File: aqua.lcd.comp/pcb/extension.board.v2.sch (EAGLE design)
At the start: 50 parts, among them IC1 NCP1117ST50T3G, K2 JS-M1-9V-4, Q1 BC447, T1 IRFR024NPBF, T10 BC847BSMD, T11 IRFR024NPBF, T12 BC847BSMD, T2 BC847BSMD, T3 IRFR024NPBF, T4 BC847BSMD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

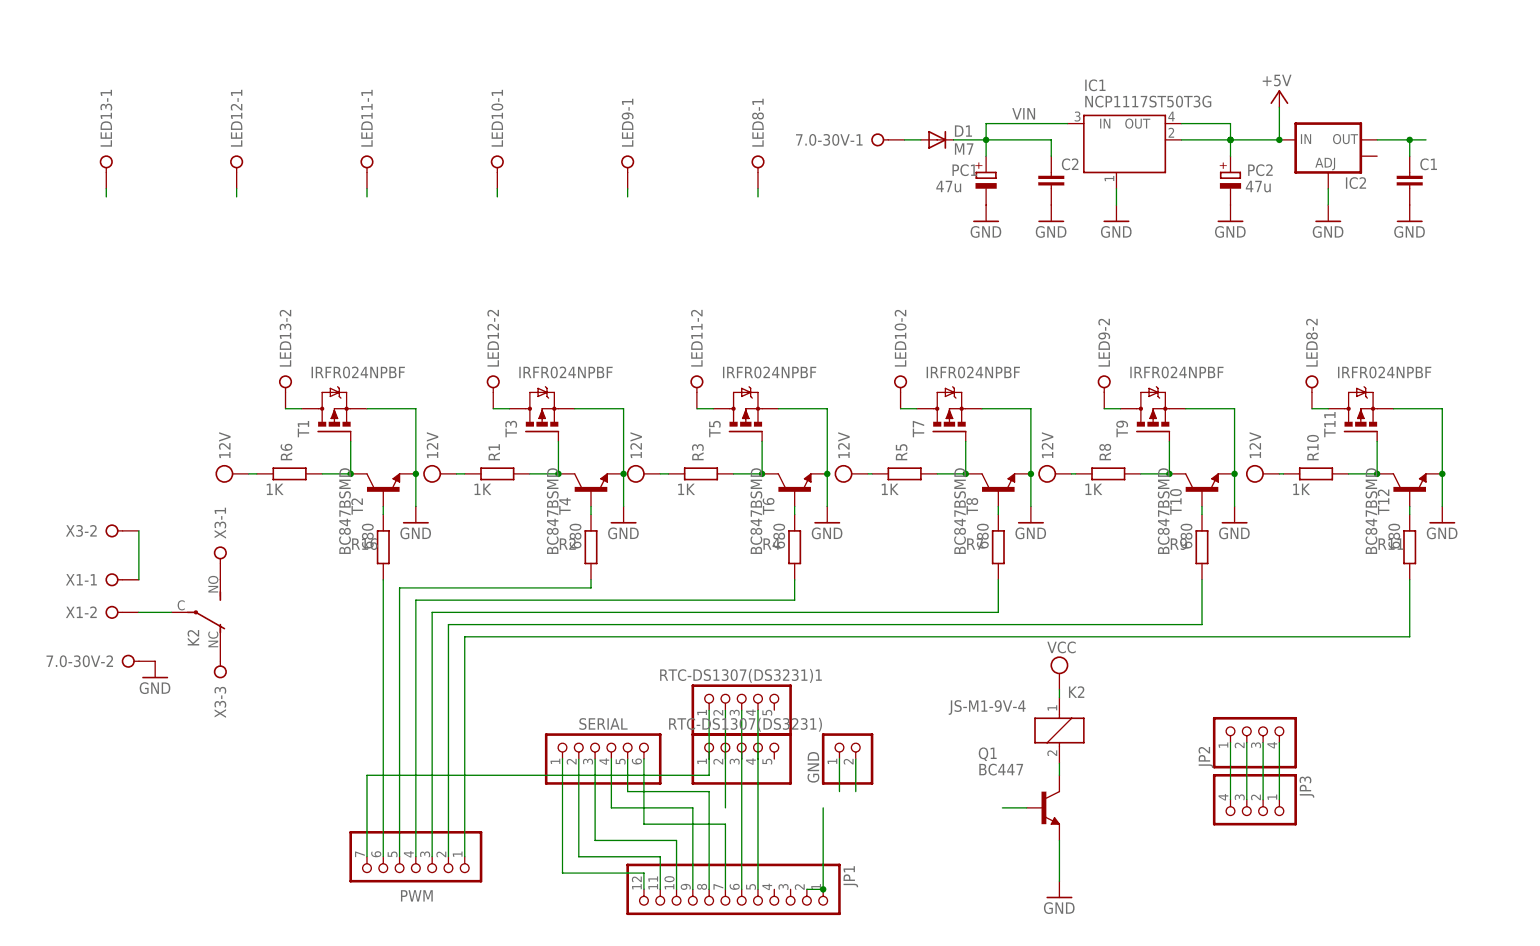
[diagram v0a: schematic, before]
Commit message: extension board modified
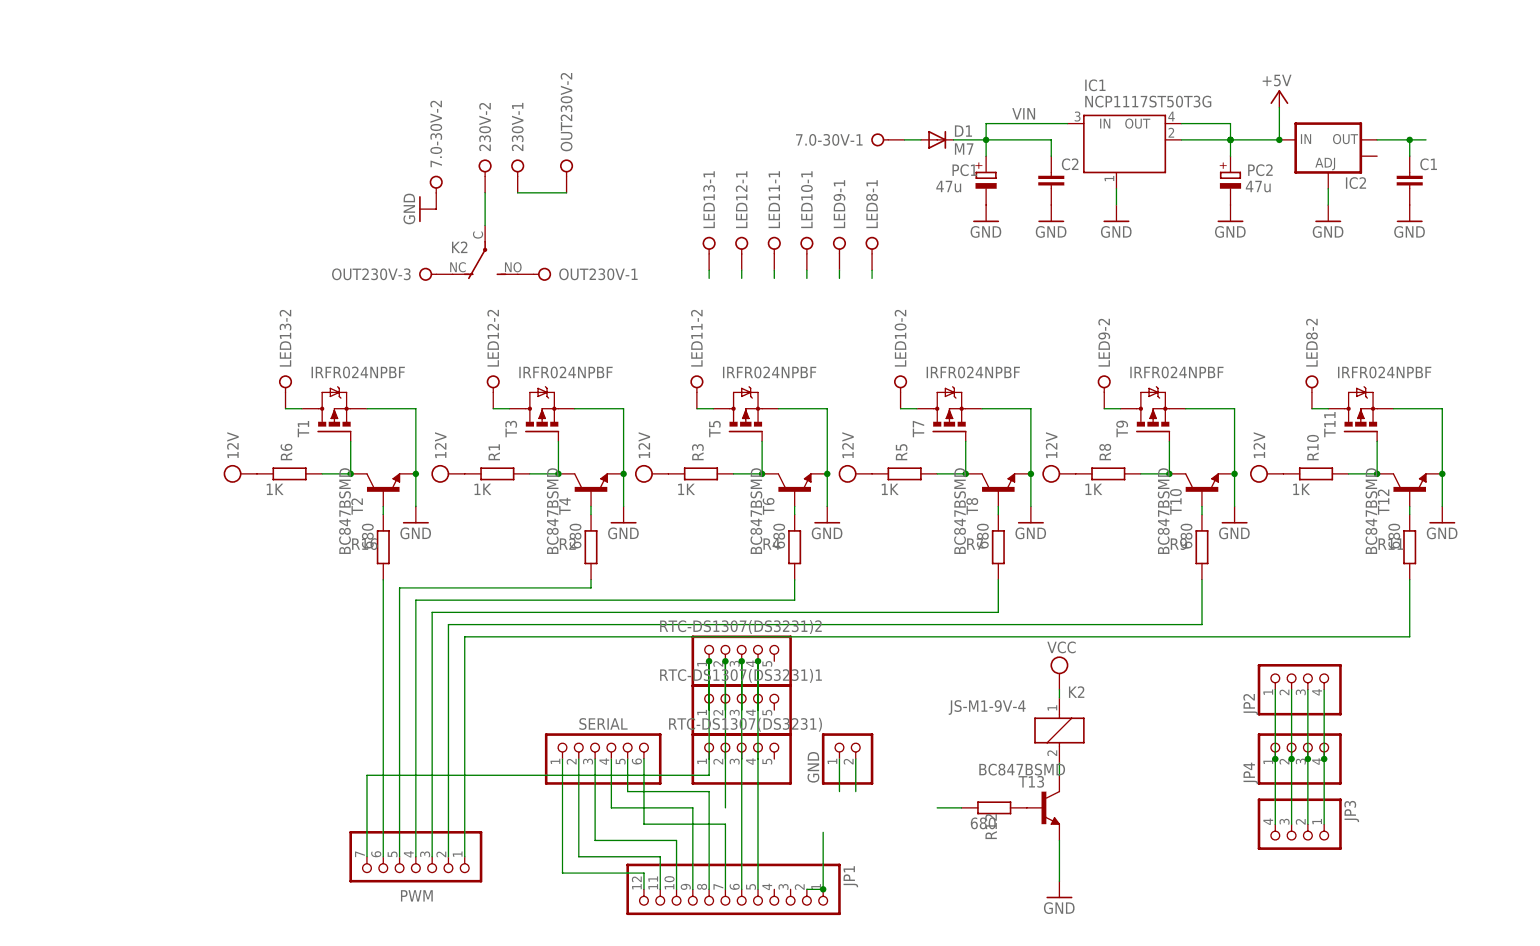
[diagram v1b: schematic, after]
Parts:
- removed Q1: BC447, transistor-npn:BC447
- removed X1: (no value), con-wago-508:W237-02P
- removed X3: (no value), con-wago-508:W237-3E
- added 230V: (no value), con-wago-508:W237-02P
- added JP4: (no value), pinhead:PINHD-1X4
- added OUT230V: (no value), con-wago-508:W237-3E
- added R12: 680, rcl:R-EU_R1206
- added RTC-DS1307(DS3231)2: (no value), pinhead:PINHD-1X5
- added T13: BC847BSMD, transistor-npn:BC847BSMD
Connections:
- new net N$34: R12.2, T13.B
- net +5V: now also JP4.1
- net 3.3V: now also RTC-DS1307(DS3231)2.2
- net GND: now also JP4.3, RTC-DS1307(DS3231)2.1, T13.E; no longer Q1.E
- net N$1: now also 230V-1.KL, OUT230V-2.KL; no longer X1-1.KL, X3-2.KL
- net N$14: now also OUT230V-1.KL; no longer X3-1.KL
- net N$2: now also 230V-2.KL; no longer X1-2.KL
- net N$26: now also JP4.4
- net N$37: now also OUT230V-3.KL; no longer X3-3.KL
- net N$41: now also T13.C; no longer Q1.C
- net OUT: now also JP4.2
- net SCL: now also RTC-DS1307(DS3231)2.4
- net SDA: now also RTC-DS1307(DS3231)2.3
- net TX3: now also R12.1; no longer Q1.B
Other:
- moved on the sheet: 7.0-30V-2, JP2, JP3, K2, LED10-1, LED11-1, LED12-1, LED13-1, LED8-1, LED9-1

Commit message: add temperature reading
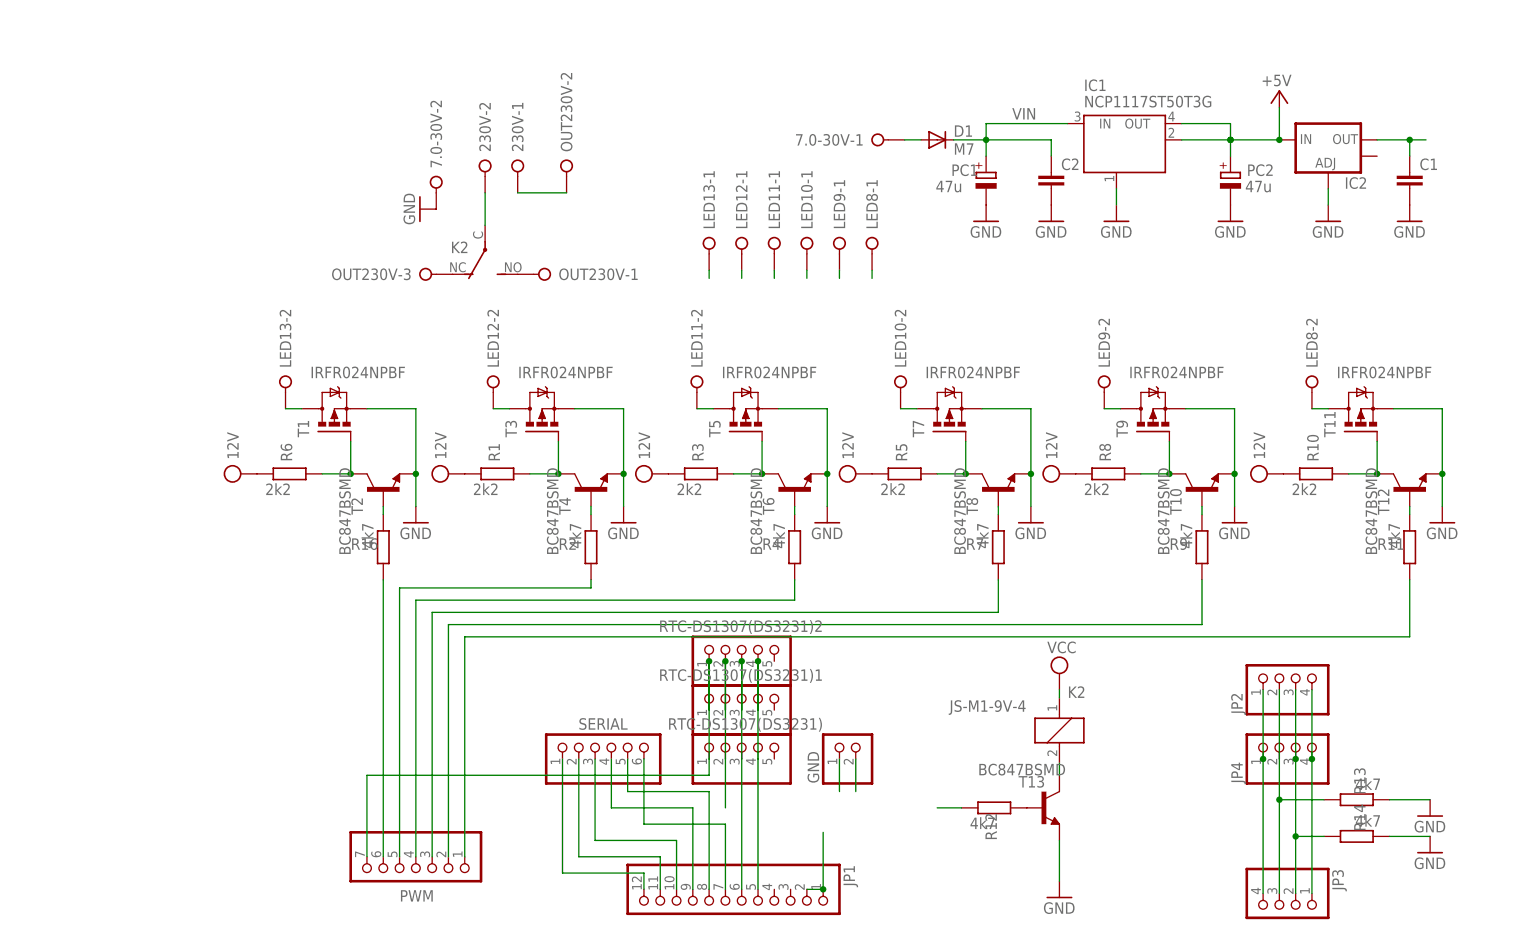
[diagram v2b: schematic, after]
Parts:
- added R13, R14: 4k7, rcl:R-EU_R1206
- R1, R10, R3, R5, R6, R8: value 1K -> 2k2
- R11, R12, R16, R2, R4, R7, R9: value 680 -> 4k7
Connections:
- removed net N$26: JP2.4, JP3.1, JP4.4
- removed net OUT: JP2.2, JP3.3, JP4.2
- new net A0: JP2.2, JP3.3, JP4.2, R13.2
- new net A1: JP2.3, JP3.2, JP4.3, R14.2
- net GND: now also JP2.4, JP3.1, JP4.4, R13.1, R14.1; no longer JP2.3, JP3.2, JP4.3
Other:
- moved on the sheet: JP2, JP3, JP4

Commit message: add thermistor
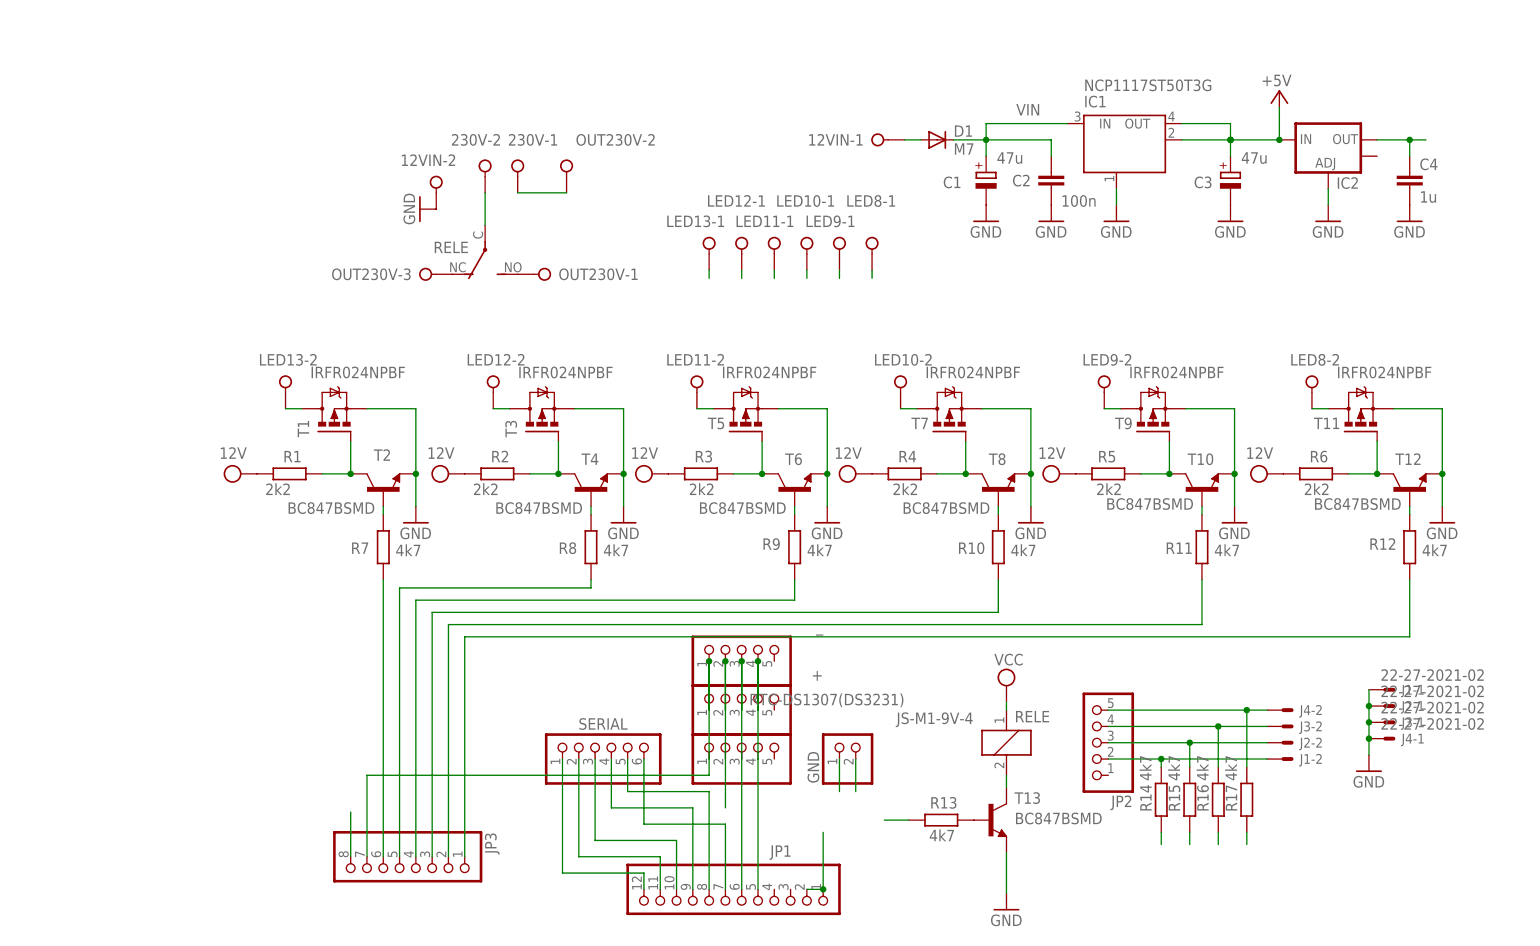
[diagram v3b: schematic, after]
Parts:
- removed JP4: (no value), pinhead:PINHD-1X4
- removed K2: JS-M1-9V-4, relay:JS-M1-9V-4
- removed PC1: 47u, rcl:CPOL-EUD
- removed PWM: (no value), pinhead:PINHD-1X7
- added C4: 1u, rcl:C-EUC0805
- added J1, J2, J3, J4: 22-27-2021-02, con-molex:22-27-2021-02
- added R15, R17: 4k7, rcl:R-EU_R1206
- added RELE: JS-M1-9V-4, relay:JS-M1-9V-4
- C1: value (none) -> 47u; device rcl:C-EUC0805 -> rcl:CPOL-EUD
- C2: value (none) -> 100n
- JP2: device pinhead:PINHD-1X4 -> pinhead:PINHD-1X5
- JP3: device pinhead:PINHD-1X4 -> pinhead:PINHD-1X8
- R10, R8: value 2k2 -> 4k7
- R2, R4: value 4k7 -> 2k2
- renumbered 7.0-30V to 12VIN, PC2 to C3, RTC-DS1307(DS3231)1 to +, RTC-DS1307(DS3231)2 to _
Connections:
- removed net A0: JP2.2, JP3.3, JP4.2, R13.2
- removed net A1: JP2.3, JP3.2, JP4.3, R14.2
- new net N$26: J4-2.S, JP2.5, R17.1
- new net N$39: J3-2.S, JP2.4, R16.1
- new net N$43: J1-2.S, JP2.2, R14.1
- new net N$45: J2-2.S, JP2.3, R15.1
- new net VCC: R4.1
- net +5V: now also RELE1.1; no longer JP2.1, JP3.4, JP4.1, K21.1
- net 3.3V: now also C4.1, JP3.8, R14.2, R15.2, R16.2, R17.2; no longer C1.1
- net GND: now also C1.-, C4.2, J1-1.S, J2-1.S, J3-1.S, J4-1.S, JP3.7; no longer C1.2, JP2.4, JP3.1, JP4.4, PC1.-, PWM.7, R13.1, R14.1
- net N$10: now also JP3.6, R7.2; no longer PWM.6, R16.2
- net N$11: now also R7.1; no longer R16.1
- net N$12: now also R1.2; no longer R6.2
- net N$14: now also RELE2.S; no longer K22.S
- net N$15: now also R8.1; no longer R2.1
- net N$16: now also R2.2; no longer R1.2
- net N$18: now also R9.1; no longer R4.1
- net N$2: now also RELE2.P; no longer K22.P
- net N$21: now also R10.1; no longer R7.1
- net N$22: now also R4.2; no longer R5.2
- net N$28: now also R11.1; no longer R9.1
- net N$29: now also R5.2; no longer R8.2
- net N$31: now also R12.1; no longer R11.1
- net N$32: now also R6.2; no longer R10.2
- net N$34: now also R13.2; no longer R12.2
- net N$37: now also RELE2.O; no longer K22.O
- net N$41: now also RELE1.2; no longer K21.2
- net N$5: now also JP3.1, R12.2; no longer PWM.1, R11.2
- net N$6: now also JP3.2, R11.2; no longer PWM.2, R9.2
- net N$7: now also JP3.3, R10.2; no longer PWM.3, R7.2
- net N$8: now also JP3.4, R9.2; no longer PWM.4, R4.2
- net N$9: now also JP3.5, R8.2; no longer PWM.5, R2.2
- net PWRIN: now also R2.1; no longer R10.1, R8.1
- net TX3: now also R13.1; no longer R12.1
- net VIN: now also C1.+; no longer PC1.+
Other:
- moved on the sheet: R1, R10, R11, R12, R13, R14, R16, R2, R4, R5, R6, R7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

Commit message: fix button local colors
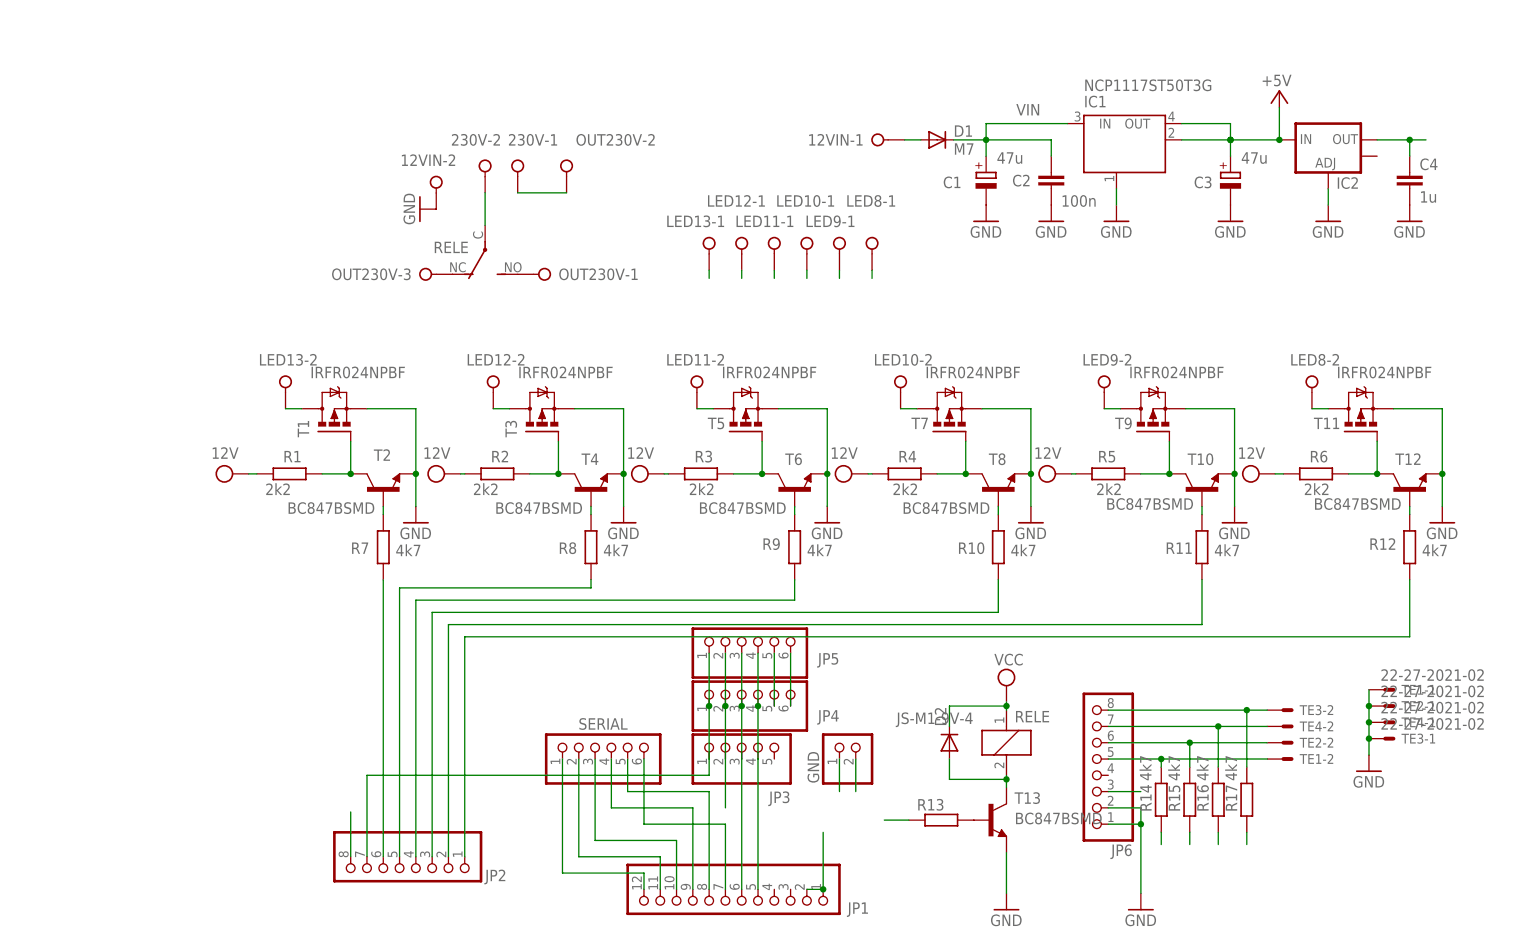
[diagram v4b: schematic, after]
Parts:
- removed +, RTC-DS1307(DS3231), _: (no value), pinhead:PINHD-1X5
- added D2: (no value), diode:DIODE-DO-214AC
- added JP4, JP5: (no value), pinhead:PINHD-1X6
- added JP6: (no value), pinhead:PINHD-1X8
- JP2: device pinhead:PINHD-1X5 -> pinhead:PINHD-1X8
- JP3: device pinhead:PINHD-1X8 -> pinhead:PINHD-1X5
- R13: value 4k7 -> (none); device rcl:R-EU_R1206 -> rcl:R-EU_0207/15
- renumbered J1 to TE1, J2 to TE2, J3 to TE4, J4 to TE3
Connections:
- removed net VCC: R4.1
- new net N$46: JP4.5, JP5.5
- new net N$47: JP4.6, JP5.6
- net +5V: now also D2.C
- net 3.3V: now also JP2.8, JP3.2, JP4.2, JP5.2; no longer +.2, JP3.8, RTC-DS1307(DS3231).2, _.2
- net GND: now also JP2.7, JP3.1, JP4.1, JP5.1, JP6.1, JP6.2; no longer +.1, JP3.7, RTC-DS1307(DS3231).1, _.1
- net N$10: now also JP2.6; no longer JP3.6
- net N$26: now also JP6.8; no longer JP2.5
- net N$39: now also JP6.7; no longer JP2.4
- net N$41: now also D2.A
- net N$43: now also JP6.5; no longer JP2.2
- net N$45: now also JP6.6; no longer JP2.3
- net N$5: now also JP2.1; no longer JP3.1
- net N$6: now also JP2.2; no longer JP3.2
- net N$7: now also JP2.3; no longer JP3.3
- net N$8: now also JP2.4; no longer JP3.4
- net N$9: now also JP2.5; no longer JP3.5
- net PWRIN: no longer R1.1, R2.1, R3.1, R5.1, R6.1
- net SCL: now also JP3.4, JP4.4, JP5.4; no longer +.4, RTC-DS1307(DS3231).4, _.4
- net SDA: now also JP3.3, JP4.3, JP5.3; no longer +.3, RTC-DS1307(DS3231).3, _.3
- net VIN: now also JP6.3, R1.1, R2.1, R3.1, R4.1, R5.1, R6.1
